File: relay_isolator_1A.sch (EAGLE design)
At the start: 10 parts

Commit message: update git hash
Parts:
- GIT1: value b4936b8 -> eb39e18
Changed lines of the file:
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@@
 <part name="SUPPLY1" library="mylib" deviceset="GND" device=""/>
 <part name="SUPPLY2" library="mylib" deviceset="GND" device=""/>
-<part name="GIT1" library="git-revision" deviceset="GIT-REVISION" device="_1.7" value="b4936b8"/>
+<part name="GIT1" library="git-revision" deviceset="GIT-REVISION" device="_1.7" value="eb39e18"/>
 </parts>
 <sheets>

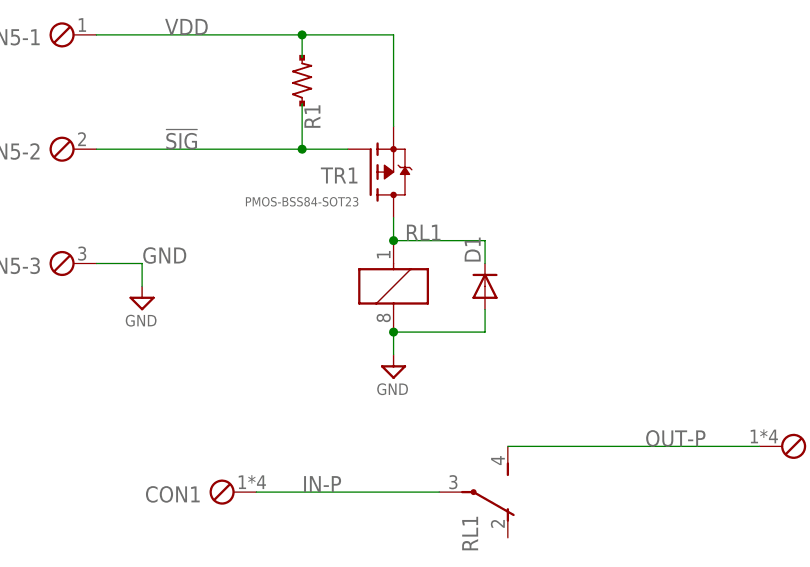
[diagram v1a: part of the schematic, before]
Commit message: update layout and library
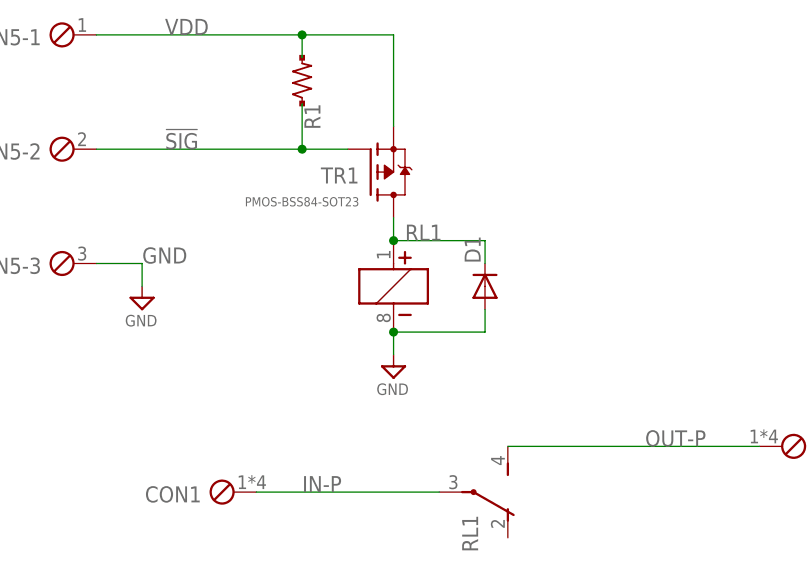
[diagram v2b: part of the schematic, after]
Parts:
- RL1: device mylib:RELAY-2C-DC5-1A -> mylib:RELAY-2C-POL-5V-G6K-2P
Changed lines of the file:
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@@
 <part name="R1" library="mylib" deviceset="R-US-*" device="-1608" technology="10K"/>
 <part name="D1" library="mylib" deviceset="DIODE2-*" device="-SOD123" technology="100V0.3A"/>
-<part name="RL1" library="mylib" deviceset="RELAY-2C-*" device="-1A" technology="DC5"/>
+<part name="RL1" library="mylib" deviceset="RELAY-2C-POL-*" device="-G6K-2P" technology="5V"/>
 <part name="SUPPLY1" library="mylib" deviceset="GND" device=""/>
 <part name="SUPPLY2" library="mylib" deviceset="GND" device=""/>

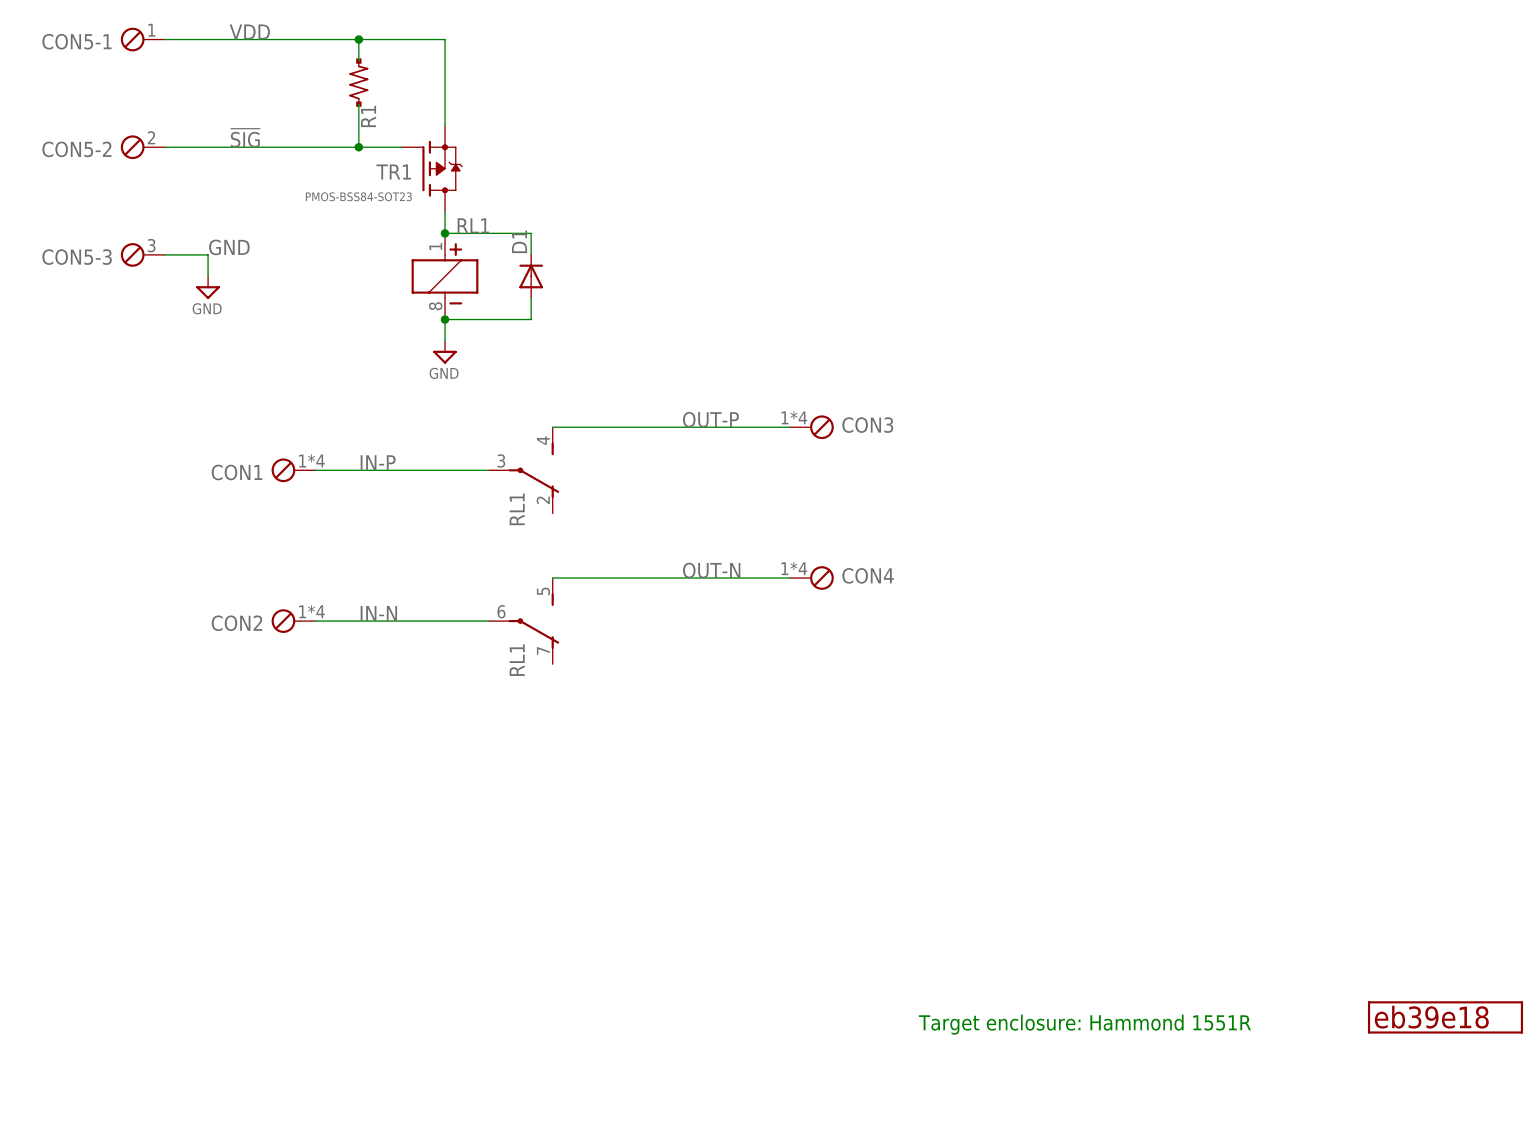
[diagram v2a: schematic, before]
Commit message: add T-6530 and POMONA72918 reference modules
- update library
- apply lib update for relay
- update relay and diode traces
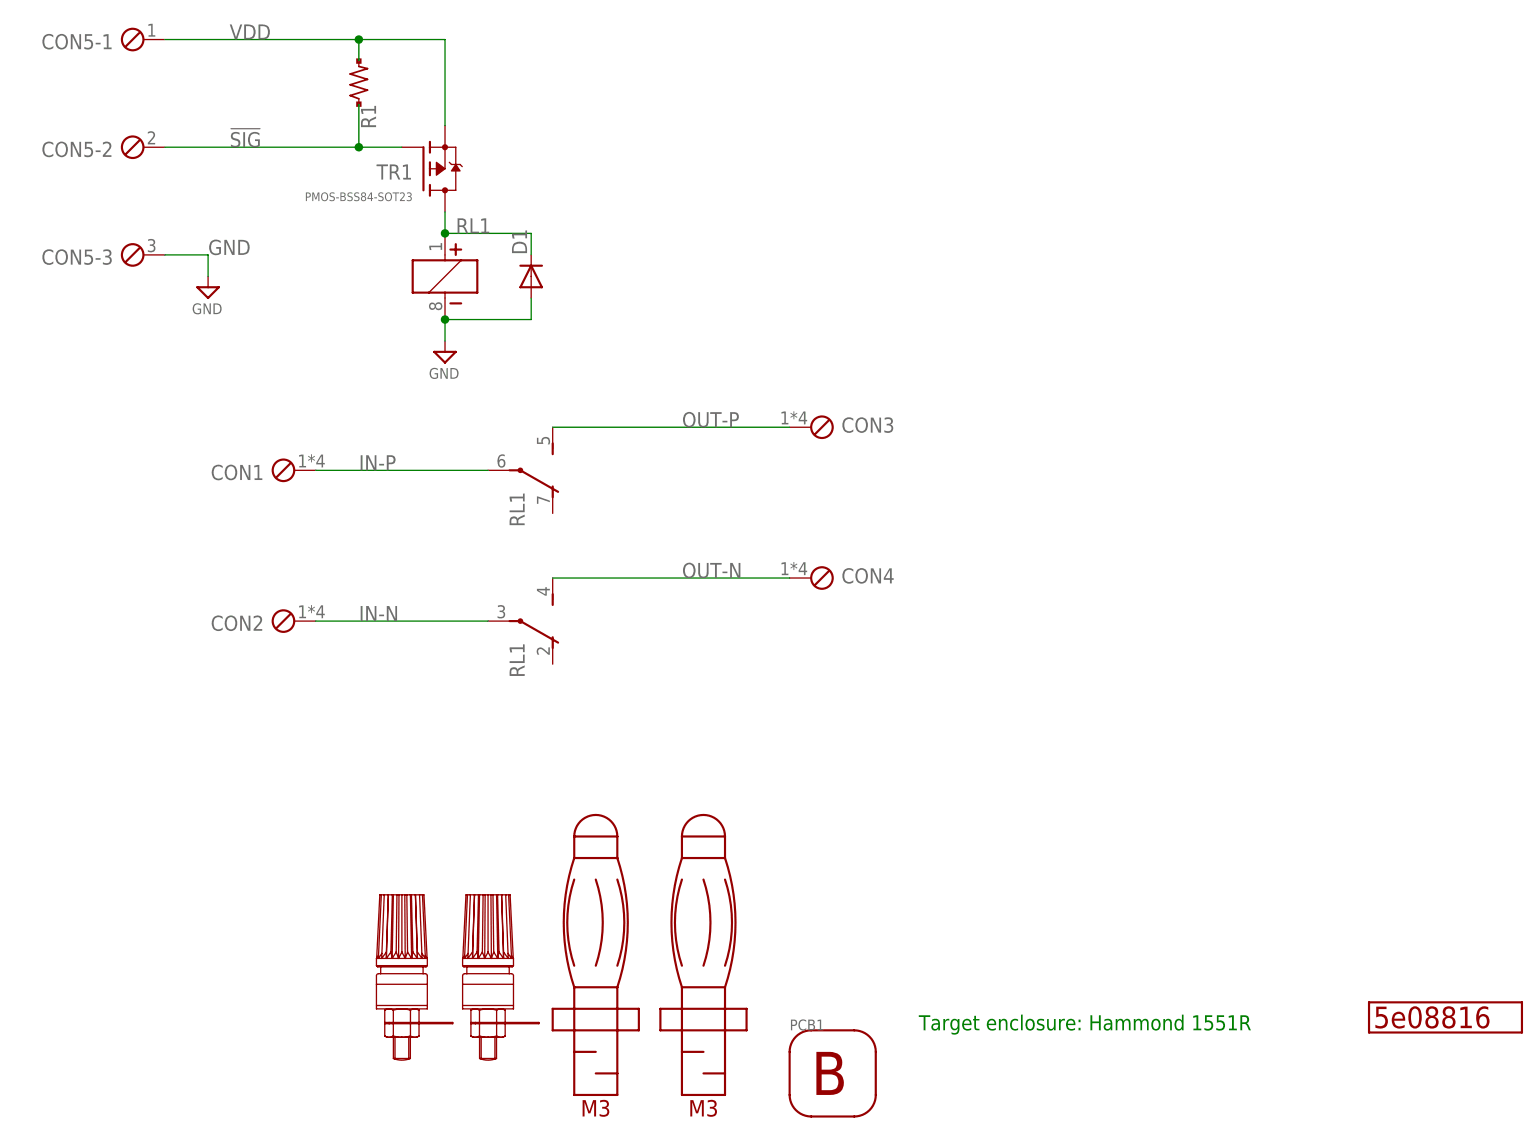
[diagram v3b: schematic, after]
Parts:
- added PCB1: (no value), mylib:HAMMOND-PCB-BK-1551R
- added REF1, REF2: POMONA72918, mylib:POMONA72918
- added REF3, REF4: T-6530, mylib:T-6530
- GIT1: value eb39e18 -> 5e08816
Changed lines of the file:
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@@
 <part name="SUPPLY1" library="mylib" deviceset="GND" device=""/>
 <part name="SUPPLY2" library="mylib" deviceset="GND" device=""/>
-<part name="GIT1" library="git-revision" deviceset="GIT-REVISION" device="_1.7" value="eb39e18"/>
+<part name="GIT1" library="git-revision" deviceset="GIT-REVISION" device="_1.7" value="5e08816"/>
+<part name="PCB1" library="mylib" deviceset="HAMMOND-PCB-*" device="-1551R" technology="BK"/>
+<part name="REF1" library="mylib" deviceset="POMONA72918" device=""/>
+<part name="REF2" library="mylib" deviceset="POMONA72918" device=""/>
+<part name="REF3" library="mylib" deviceset="T-6530" device=""/>
+<part name="REF4" library="mylib" deviceset="T-6530" device=""/>
 </parts>
 <sheets>
@@
 <instance part="RL1" gate="G$2" x="114.3" y="86.36" rot="R270"/>
 <instance part="RL1" gate="G$3" x="114.3" y="68.58" rot="R270"/>
+<instance part="PCB1" gate="G$1" x="147.32" y="10.16"/>
+<instance part="REF1" gate="G$1" x="137.16" y="20.32"/>
+<instance part="REF2" gate="G$1" x="124.46" y="20.32"/>
+<instance part="REF3" gate="G$1" x="111.76" y="22.86"/>
+<instance part="REF4" gate="G$1" x="101.6" y="22.86"/>
 </instances>
 <busses>

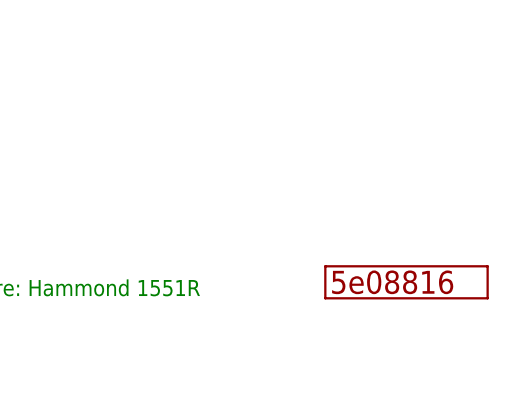
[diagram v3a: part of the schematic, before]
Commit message: all components on top mount
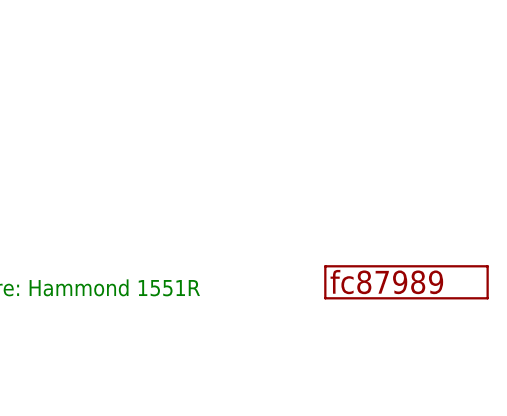
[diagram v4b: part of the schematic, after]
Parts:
- GIT1: value 5e08816 -> fc87989
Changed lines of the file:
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@@
 <part name="SUPPLY1" library="mylib" deviceset="GND" device=""/>
 <part name="SUPPLY2" library="mylib" deviceset="GND" device=""/>
-<part name="GIT1" library="git-revision" deviceset="GIT-REVISION" device="_1.7" value="5e08816"/>
+<part name="GIT1" library="git-revision" deviceset="GIT-REVISION" device="_1.7" value="fc87989"/>
 <part name="PCB1" library="mylib" deviceset="HAMMOND-PCB-*" device="-1551R" technology="BK"/>
 <part name="REF1" library="mylib" deviceset="POMONA72918" device=""/>
